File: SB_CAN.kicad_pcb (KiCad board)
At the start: 4 copper layers, 53.3 x 40.2 mm, 88 parts, among them J1 XT30PB_IN, J2 USB_C_Receptacle_USB2.0_16P, J3 Excluder, J4 PT100, J5 Hotend, J6 FAN2, J7 LDC, J8 FS, J9 Conn_02x05_Odd_Even, Q1 BUK9M8R5-40EX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

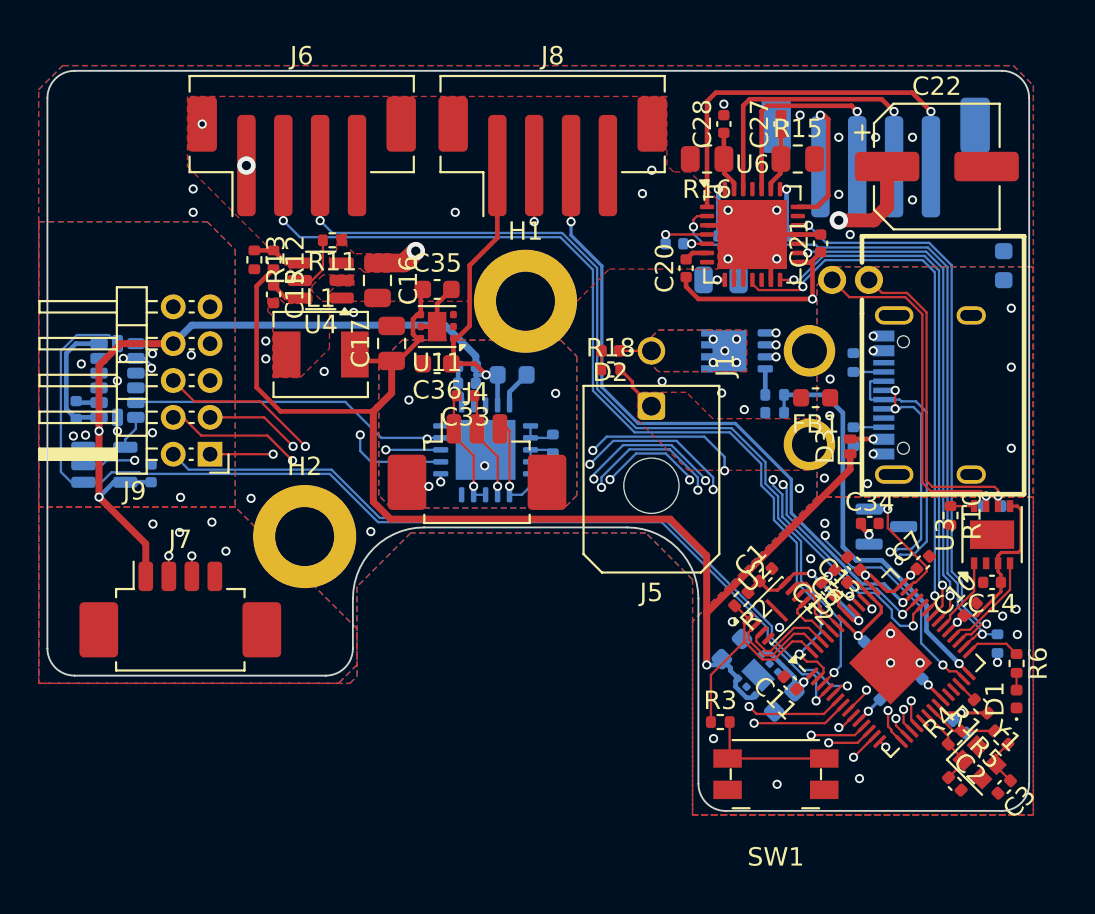
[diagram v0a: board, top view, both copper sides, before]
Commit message: layout: optmise +3v3A power source: use new 3d models
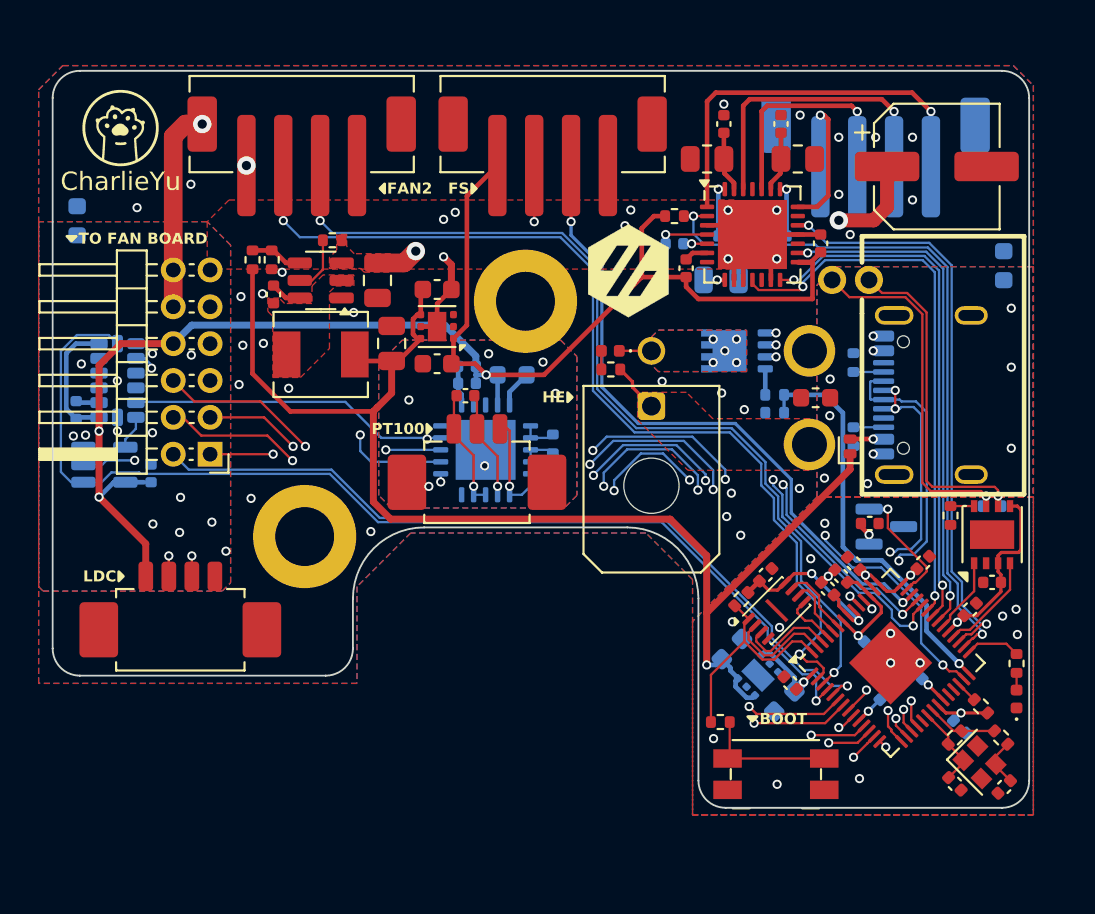
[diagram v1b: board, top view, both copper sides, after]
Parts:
- added FB4: 120R@100MHz, Inductor_SMD:L_0603_1608Metric, B.Cu at (104.6, 110.2)
- added REF**: Voron Hex, Logos:Voron_Logo_Hex, F.Cu at (110.9, 104.5)
- added RFF**: CharlieYu, Logos:charlieyu, F.Cu at (83.3, 96.8)
- J2: footprint Connector_USB:USB_C_Receptacle_XKB_U262-16XN-4BVC11 -> Connector_USB:USB_C_Receptacle_GCT_USB4105-xx-A_16P_TopMnt_Horizontal
- J5: footprint Connector_Molex:Molex_Micro-Fit_3.0_43045-0200_2x01_P3.00mm_Horizontal -> Library:Molex_Micro-Fit_3.0_43045-0200_2x01_P3.00mm_Horizontal
- J9: value Conn_02x05_Odd_Even -> FAN; footprint Connector_PinHeader_2.00mm:PinHeader_2x05_P2.00mm_Horizontal -> Connector_PinHeader_2.00mm:PinHeader_2x06_P2.00mm_Horizontal
- R14: moved to F.Cu
- moved R14 29.1 mm to (113.4, 101.6), turned to 0 degrees
- moved FB3 25.0 mm to (81.0, 101.8), turned to 90 degrees
- moved R12 1.14 mm to (90.5, 103.9)
- moved R13 0.94 mm to (91.5, 103.9)
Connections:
- C20 pad 1: +3V3A -> +3V3B
- C21 pad 1: +3V3A -> +3V3B
- FB3 pad 1: +3V3B -> GND
- FB3 pad 2: Net-(U9-VDD) -> PGND
- H1 pad 1: GND -> PGND
- H2 pad 1: GND -> PGND
- J6 pad MP: GND -> PGND
- J7 pad MP: GND -> PGND
- J8 pad MP: GND -> PGND
- J9 pad 10: GND -> PGND
- J9 pad 9: +24V -> GND
- R14 pad 1: +3V3A -> +3V3B
- U6 pad 15: +3V3A -> +3V3B
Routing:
- net +3V3B: track 63.9 -> 92.9 mm
- net +3V3A: track 70.1 -> 43.0 mm, vias 11 -> 9
- net PGND: track 0.00 -> 11.1 mm, vias 23 -> 31
- net GND: track 33.9 -> 25.3 mm, vias 46 -> 49
- net +24V: track 74.3 -> 72.3 mm
- net /ADXL_INT1: track 55.6 -> 54.8 mm, vias 3 -> 2
- net /ENDSTOP0: track 42.9 -> 42.1 mm
- net /SPI0_CS2: track 43.1 -> 42.3 mm
- net +5V: track 70.5 -> 69.9 mm
- removed copper zone on In1.Cu, net +24V
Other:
- board size 53.3 x 40.2 mm -> 53 x 40 mm
- board text added: "BOOT"
- board text added: "FAN2"
- board text added: "FS"
- board text added: "HE"
- board text added: "LDC"
- board text added: "PT100"
- board text added: "TO FAN BOARD"
